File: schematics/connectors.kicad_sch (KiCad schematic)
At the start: 4 parts, among them J2 SWD, J3 Micro_SD_Card_Det1

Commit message: Update the board schematics
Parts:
- removed J2: SWD, Connector_PinHeader_2.54mm:PinHeader_1x04_P2.54mm_Vertical, symbol Connector:Conn_01x04_Pin
- removed J?: Conn_SNP59_96_32X3, Custom:SNP59-96, symbol Custom:SNP59-96
- added C3: 100nF, Capacitor_SMD:C_0603_1608Metric, symbol Device:C
- added J4: SWD, Connector_PinHeader_1.27mm:PinHeader_2x07_P1.27mm_Vertical_SMD, symbol Connector:Conn_ST_STDC14
- added R2 (x4): 10k, Resistor_SMD:R_0603_1608Metric, symbol Device:R
- added SW1: RESET, Button_Switch_THT:SW_PUSH_6mm_H4.3mm, symbol Switch:SW_SPST
- J3: value Micro_SD_Card_Det1 -> Micro SD Card
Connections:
- net +3.3V: now also J4.3 (VCC), R2.1, R2.1, R2.1
- net GND: now also C3.2, J4.11 (GNDDetect), J4.5 (GND), J4.7 (GND), R2.2, SW1.2 (B)
- net SWCLK: now also J4.6 (JCLK/SWCLK), R2.1
- net SWDIO: now also J4.4 (JTMS/SWDIO), R2.2
- new net NRST: C3.1, J4.12 (~{RST}), R2.2, SW1.1 (A)
- new net SWO: J4.8 (JTDO/SWO), R2.2
- no-connect marks 93 -> 7
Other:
- note removed: "2K Interface"
- moved on the sheet: J3, R4

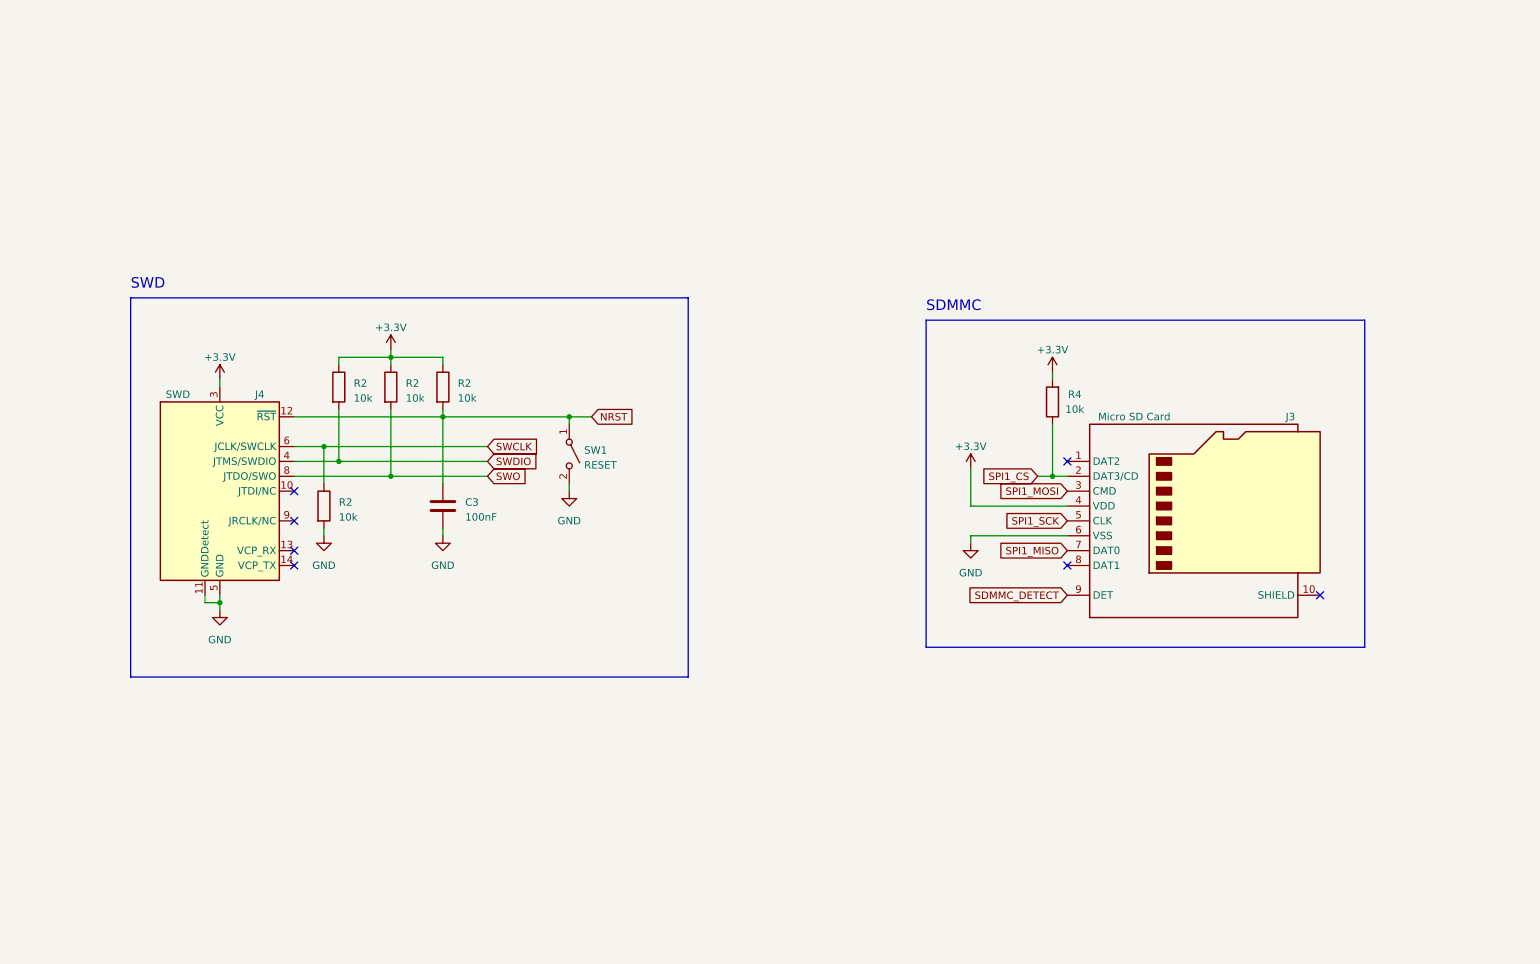
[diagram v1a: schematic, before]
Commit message: Re-route data buses and add heap allocator
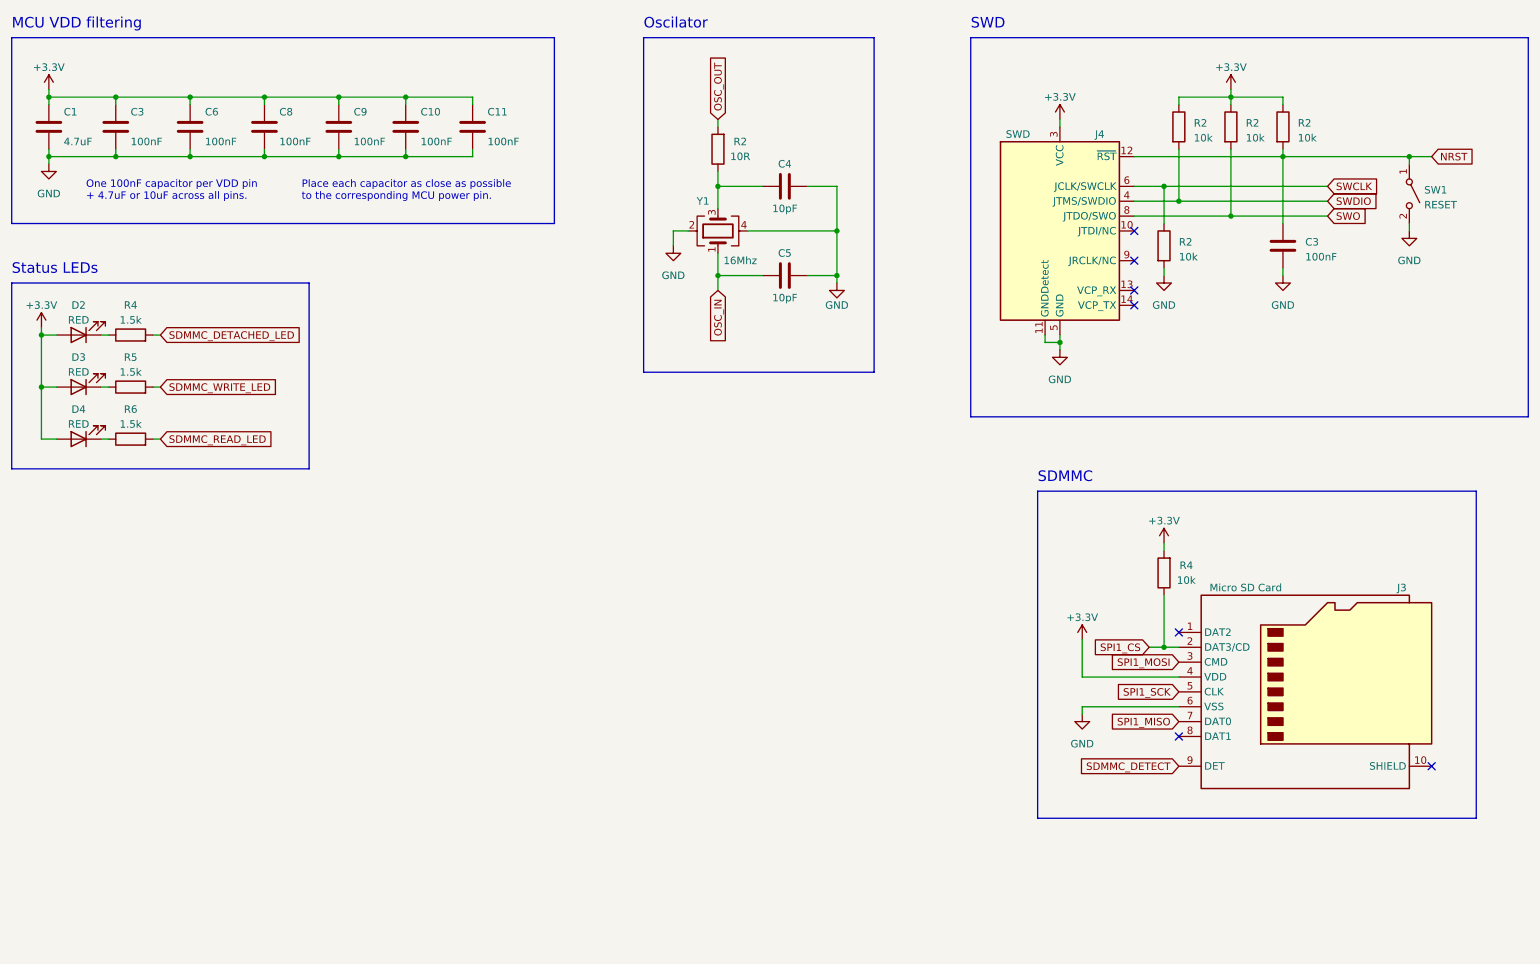
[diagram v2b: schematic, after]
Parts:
- added C1: 4.7uF, Capacitor_SMD:C_0603_1608Metric, symbol Device:C
- added C10, C11, C3, C6, C8, C9: 100nF, Capacitor_SMD:C_0603_1608Metric, symbol Device:C
- added C4, C5: 10pF, Capacitor_SMD:C_0603_1608Metric, symbol Device:C
- added D2, D3, D4: RED, LED_SMD:LED_0603_1608Metric, symbol Device:LED
- added R2: 10R, Resistor_SMD:R_0603_1608Metric, symbol Device:R
- added R4, R5, R6: 1.5k, Resistor_SMD:R_0603_1608Metric, symbol Device:R
- added Y1: 16Mhz, Crystal:Crystal_SMD_3225-4Pin_3.2x2.5mm, symbol Device:Crystal_GND24
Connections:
- net +3.3V: now also C1.1, C10.1, C11.1, C3.1, C6.1, C8.1, C9.1, D2.2 (A), D3.2 (A), D4.2 (A)
- net GND: now also C1.2, C10.2, C11.2, C3.2, C4.2, C5.2, C6.2, C8.2, C9.2, Y1.2, Y1.4
- new net: D4.1 (K), R6.1
- new net: C4.1, R2.1, Y1.3
- new net: D3.1 (K), R5.1
- new net: D2.1 (K), R4.1
- new net OSC_IN: C5.1, Y1.1
- new net OSC_OUT: R2.2
- new net SDMMC_DETACHED_LED: R4.2
- new net SDMMC_READ_LED: R6.2
- new net SDMMC_WRITE_LED: R5.2
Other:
- note added: "MCU VDD filtering"
- note added: "One 100nF capacitor per VDD pin + 4.7uF or 10uF across all pins."
- note added: "Oscilator"
- note added: "Place each capacitor as close as possible to the corresponding MCU power pin."
- note added: "Status LEDs"
- moved on the sheet: C3, J3, J4, R2, R4, SW1

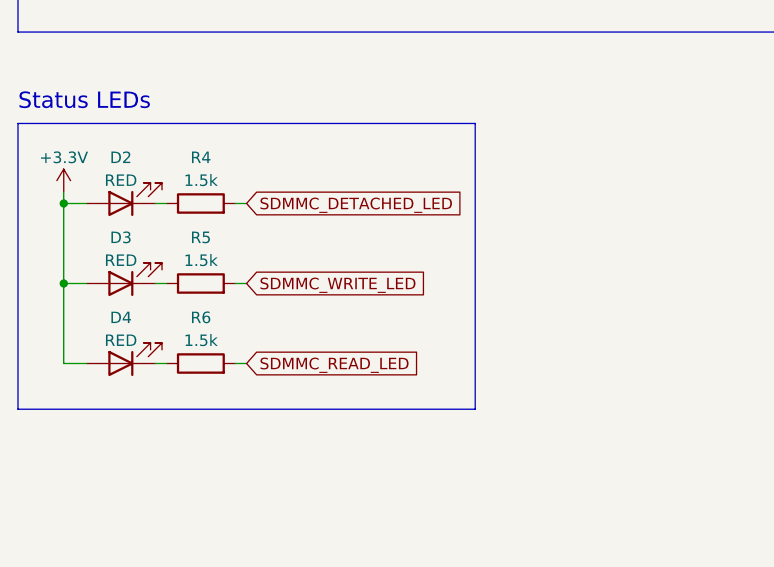
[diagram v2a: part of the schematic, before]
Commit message: Tune PCB trace spacing
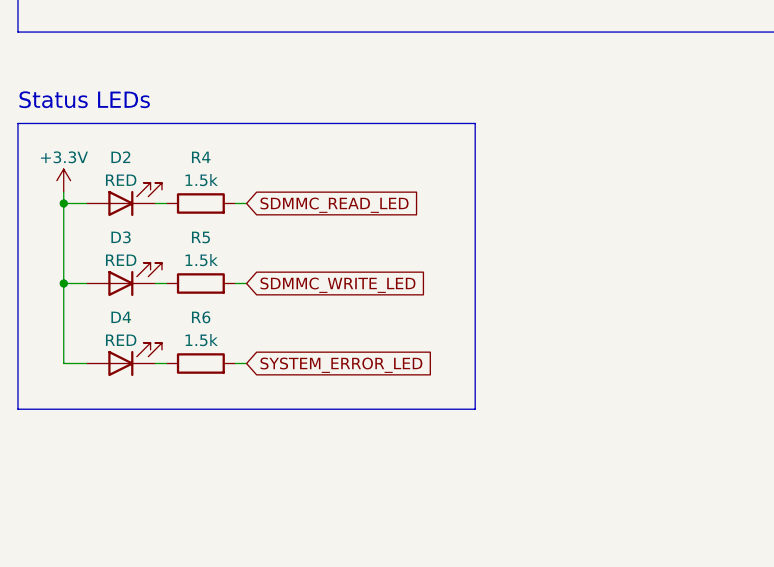
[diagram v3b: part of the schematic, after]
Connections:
- net SDMMC_DETACHED_LED is gone; now on net SDMMC_READ_LED: R4.2
- net SDMMC_READ_LED: no longer R6.2
- new net SYSTEM_ERROR_LED: R6.2
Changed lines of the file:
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@@
     )
   )
-  (global_label "SDMMC_READ_LED" (shape input) (at 43.18 87.63 0) (fields_autoplaced)
+  (global_label "SYSTEM_ERROR_LED" (shape input) (at 43.18 87.63 0) (fields_autoplaced)
     (effects (font (size 1.27 1.27)) (justify left))
-    (property "Intersheetrefs" "${INTERSHEET_REFS}" (at 62.898 87.63 0)
-      (effects (font (size 1.27 1.27)) (justify left) hide)
-    )
-  )
-  (global_label "SDMMC_DETACHED_LED" (shape input) (at 43.18 69.85 0) (fields_autoplaced)
-    (effects (font (size 1.27 1.27)) (justify left))
-    (property "Intersheetrefs" "${INTERSHEET_REFS}" (at 67.6151 69.85 0)
+    (property "Intersheetrefs" "${INTERSHEET_REFS}" (at 64.8332 87.63 0)
       (effects (font (size 1.27 1.27)) (justify left) hide)
     )
@@
     )
   )
+  (global_label "SDMMC_READ_LED" (shape input) (at 43.18 69.85 0) (fields_autoplaced)
+    (effects (font (size 1.27 1.27)) (justify left))
+    (property "Intersheetrefs" "${INTERSHEET_REFS}" (at 62.898 69.85 0)
+      (effects (font (size 1.27 1.27)) (justify left) hide)
+    )
+  )

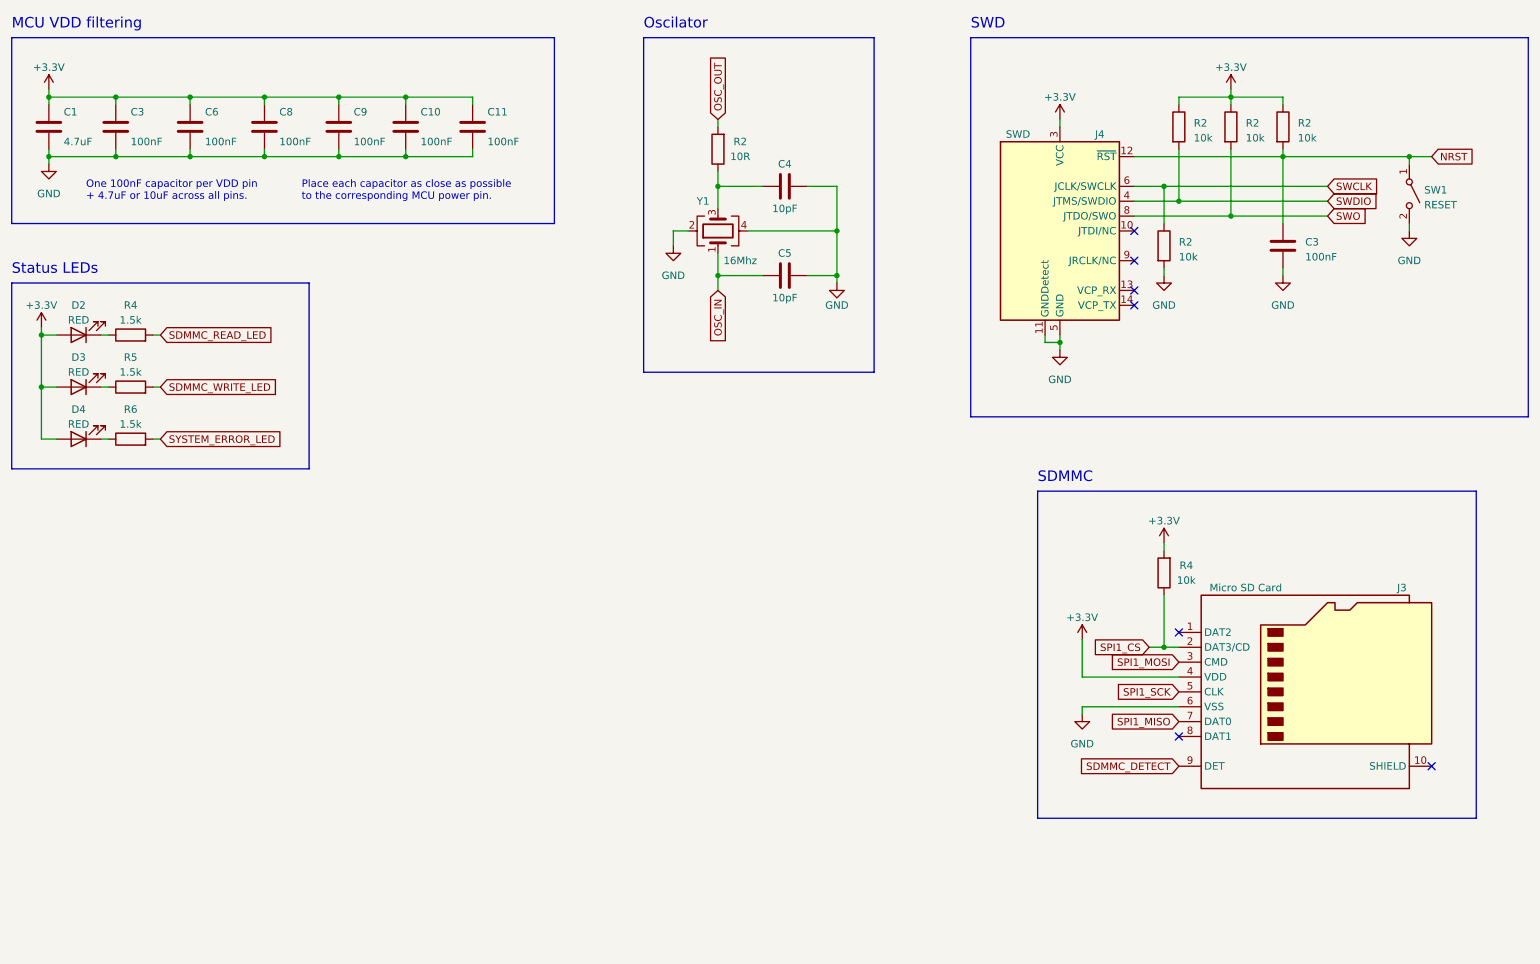
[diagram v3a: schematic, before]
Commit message: Move components to appropriate sheets
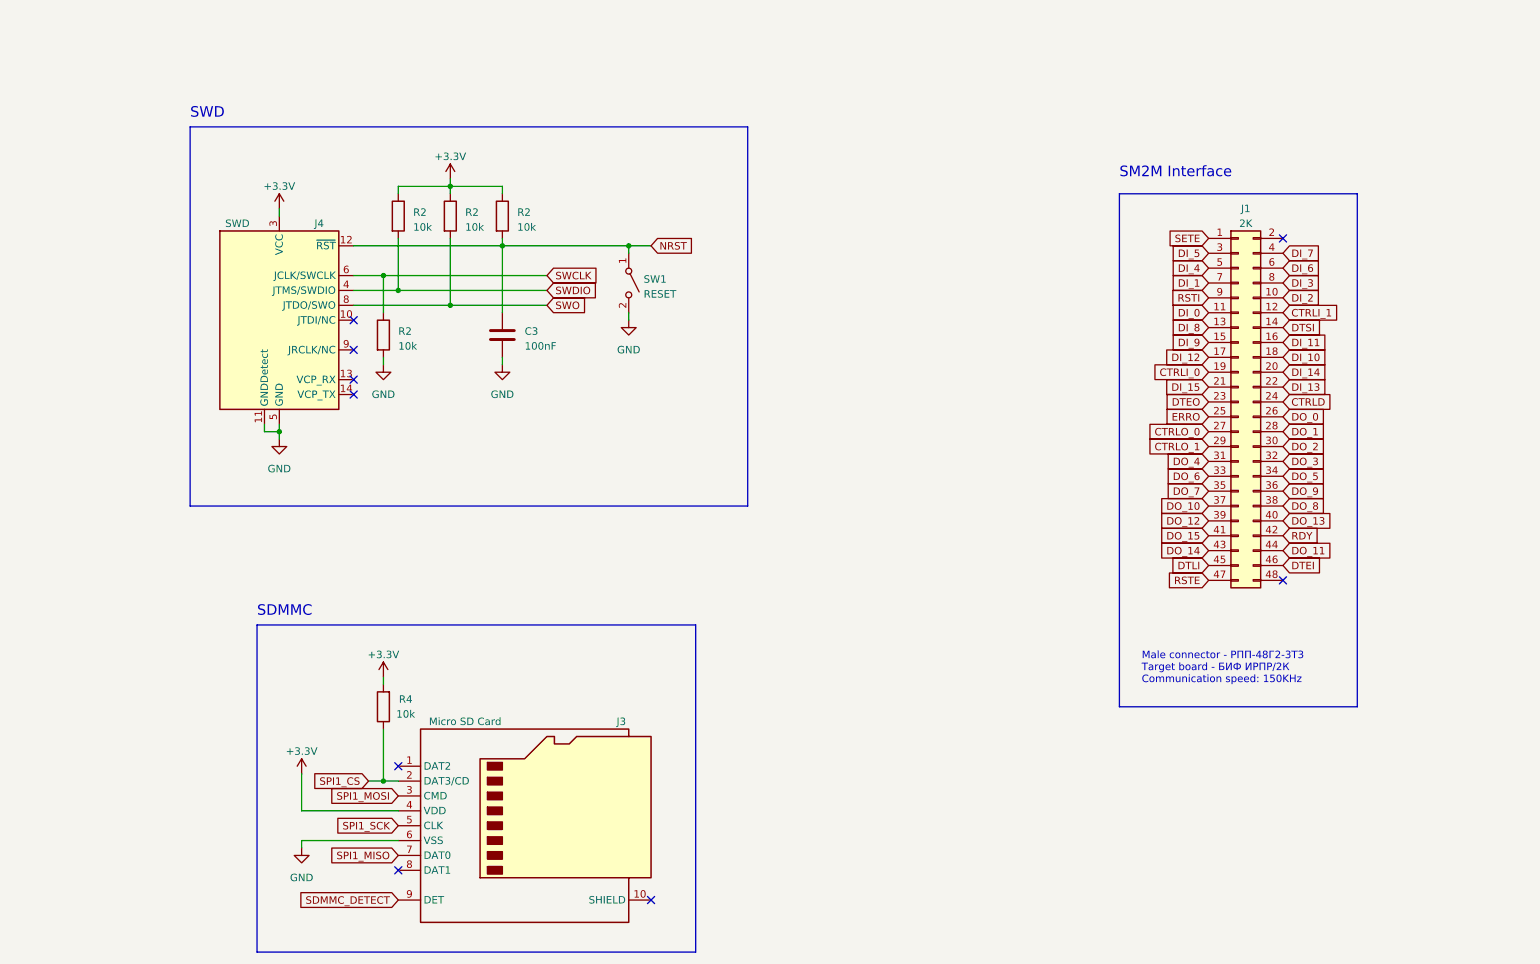
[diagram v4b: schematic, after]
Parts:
- removed C1: 4.7uF, Capacitor_SMD:C_0603_1608Metric, symbol Device:C
- removed C10, C11, C3, C6, C8, C9: 100nF, Capacitor_SMD:C_0603_1608Metric, symbol Device:C
- removed C4, C5: 10pF, Capacitor_SMD:C_0603_1608Metric, symbol Device:C
- removed D2, D3, D4: RED, LED_SMD:LED_0603_1608Metric, symbol Device:LED
- removed R2: 10R, Resistor_SMD:R_0603_1608Metric, symbol Device:R
- removed R4, R5, R6: 1.5k, Resistor_SMD:R_0603_1608Metric, symbol Device:R
- removed Y1: 16Mhz, Crystal:Crystal_SMD_3225-4Pin_3.2x2.5mm, symbol Device:Crystal_GND24
- added J1: 2K, Custom:RPP_48G2_3T3_Male, symbol Connector_Generic:Conn_02x24_Odd_Even
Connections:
- new net CTRLD: J1.24 (Pin_24)
- new net CTRLI_0: J1.19 (Pin_19)
- new net CTRLI_1: J1.12 (Pin_12)
- new net CTRLO_0: J1.27 (Pin_27)
- new net CTRLO_1: J1.29 (Pin_29)
- new net DI_0: J1.11 (Pin_11)
- new net DI_1: J1.7 (Pin_7)
- new net DI_10: J1.18 (Pin_18)
- new net DI_11: J1.16 (Pin_16)
- new net DI_12: J1.17 (Pin_17)
- new net DI_13: J1.22 (Pin_22)
- new net DI_14: J1.20 (Pin_20)
- new net DI_15: J1.21 (Pin_21)
- new net DI_2: J1.10 (Pin_10)
- new net DI_3: J1.8 (Pin_8)
- new net DI_4: J1.5 (Pin_5)
- new net DI_5: J1.3 (Pin_3)
- new net DI_6: J1.6 (Pin_6)
- new net DI_7: J1.4 (Pin_4)
- new net DI_8: J1.13 (Pin_13)
- new net DI_9: J1.15 (Pin_15)
- new net DO_0: J1.26 (Pin_26)
- new net DO_1: J1.28 (Pin_28)
- new net DO_10: J1.37 (Pin_37)
- new net DO_11: J1.44 (Pin_44)
- new net DO_12: J1.39 (Pin_39)
- new net DO_13: J1.40 (Pin_40)
- new net DO_14: J1.43 (Pin_43)
- new net DO_15: J1.41 (Pin_41)
- new net DO_2: J1.30 (Pin_30)
- new net DO_3: J1.32 (Pin_32)
- new net DO_4: J1.31 (Pin_31)
- new net DO_5: J1.34 (Pin_34)
- new net DO_6: J1.33 (Pin_33)
- new net DO_7: J1.35 (Pin_35)
- new net DO_8: J1.38 (Pin_38)
- new net DO_9: J1.36 (Pin_36)
- new net DTEI: J1.46 (Pin_46)
- new net DTEO: J1.23 (Pin_23)
- new net DTLI: J1.45 (Pin_45)
- new net DTSI: J1.14 (Pin_14)
- new net ERRO: J1.25 (Pin_25)
- new net RDY: J1.42 (Pin_42)
- new net RSTE: J1.47 (Pin_47)
- new net RSTI: J1.9 (Pin_9)
- new net SETE: J1.1 (Pin_1)
- no-connect marks 7 -> 9
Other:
- note added: "Male connector - РПП-48Г2-3Т3 Target board - БИФ ИРПР/2К Communication speed: 150KHz"
- note added: "SM2M Interface"
- note removed: "MCU VDD filtering"
- note removed: "One 100nF capacitor per VDD pin + 4.7uF or 10uF across all pins."
- note removed: "Oscilator"
- note removed: "Place each capacitor as close as possible to the corresponding MCU power pin."
- note removed: "Status LEDs"
- company: (none) -> Artem Korobko
- title: (none) -> Connectors
- moved on the sheet: C3, J3, J4, R2, R4, SW1
